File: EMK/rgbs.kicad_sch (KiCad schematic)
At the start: 0 parts

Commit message: feat: conclui a revisão 1 do EMK.
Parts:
- added C22, C23, C24, C25, C26, C27, C28, C29, C30, C31, C32, C33, C34, C35, C36, C37: 100nF, symbol Device:C
- added D20, D21, D22, D23, D24, D25, D26, D27, D28, D29, D30, D31, D32, D33, D34, D35: WS2812B, LED_SMD:LED_WS2812B_PLCC4_5.0x5.0mm_P3.2mm, symbol LED:WS2812B
- added D36: LED, symbol Device:LED
- added R12: 1K, symbol Device:R
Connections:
- new net: D33.2 (DOUT), D34.4 (DIN)
- new net: D32.2 (DOUT), D33.4 (DIN)
- new net: D20.2 (DOUT), D21.4 (DIN)
- new net: D27.2 (DOUT), D28.4 (DIN)
- new net: D26.2 (DOUT), D27.4 (DIN)
- new net: D36.2 (A), R12.1
- new net: D25.2 (DOUT), D26.4 (DIN)
- new net: D29.2 (DOUT), D30.4 (DIN)
- new net: D28.2 (DOUT), D29.4 (DIN)
- new net: D34.2 (DOUT), D35.4 (DIN)
- new net: D23.2 (DOUT), D24.4 (DIN)
- new net: D22.2 (DOUT), D23.4 (DIN)
- new net: D31.2 (DOUT), D32.4 (DIN)
- new net: D30.2 (DOUT), D31.4 (DIN)
- new net: D21.2 (DOUT), D22.4 (DIN)
- new net: D24.2 (DOUT), D25.4 (DIN)
- new net GND: C22.1, C23.1, C24.1, C25.1, C26.1, C27.1, C28.1, C29.1, C30.1, C31.1, C32.1, C33.1, C34.1, C35.1, C36.1, C37.1, D20.3 (VSS), D21.3 (VSS), D22.3 (VSS), D23.3 (VSS), D24.3 (VSS), D25.3 (VSS), D26.3 (VSS), D27.3 (VSS), D28.3 (VSS), D29.3 (VSS), D30.3 (VSS), D31.3 (VSS), D32.3 (VSS), D33.3 (VSS), D34.3 (VSS), D35.3 (VSS), D36.1 (K)
- new net ON_LED: R12.2
- new net RGB_SIG: D20.4 (DIN)
- new net RGB_VDD: C22.2, C23.2, C24.2, C25.2, C26.2, C27.2, C28.2, C29.2, C30.2, C31.2, C32.2, C33.2, C34.2, C35.2, C36.2, C37.2, D20.1 (VDD), D21.1 (VDD), D22.1 (VDD), D23.1 (VDD), D24.1 (VDD), D25.1 (VDD), D26.1 (VDD), D27.1 (VDD), D28.1 (VDD), D29.1 (VDD), D30.1 (VDD), D31.1 (VDD), D32.1 (VDD), D33.1 (VDD), D34.1 (VDD), D35.1 (VDD)

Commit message: Adiciona parte dos Footprints
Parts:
- C22, C23, C24, C25, C26, C27, C28, C29, C30, C31, C32, C33, C34, C35, C36, C37: footprint (none) -> Capacitor_SMD:C_0603_1608Metric
- D36: footprint (none) -> LED_SMD:LED_0603_1608Metric
- R12: footprint (none) -> Resistor_SMD:R_0603_1608Metric
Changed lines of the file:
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@@
 			)
 		)
-		(property "Footprint" ""
+		(property "Footprint" "Capacitor_SMD:C_0603_1608Metric"
 			(at 88.5952 64.77 0)
 			(effects
@@
 			)
 		)
-		(property "Footprint" ""
+		(property "Footprint" "Capacitor_SMD:C_0603_1608Metric"
 			(at 88.5952 101.6 0)
 			(effects
@@
 			)
 		)
-		(property "Footprint" ""
+		(property "Footprint" "Capacitor_SMD:C_0603_1608Metric"
 			(at 32.7152 138.43 0)
 			(effects
@@
 			)
 		)
-		(property "Footprint" ""
+		(property "Footprint" "Capacitor_SMD:C_0603_1608Metric"
 			(at 32.7152 64.77 0)
 			(effects
@@
 			)
 		)
-		(property "Footprint" ""
+		(property "Footprint" "Capacitor_SMD:C_0603_1608Metric"
 			(at 88.5952 27.94 0)
 			(effects
@@
 			)
 		)
-		(property "Footprint" ""
+		(property "Footprint" "Capacitor_SMD:C_0603_1608Metric"
 			(at 116.5352 27.94 0)
 			(effects
@@
 			)
 		)
-		(property "Footprint" ""
+		(property "Footprint" "LED_SMD:LED_0603_1608Metric"
 			(at 20.32 179.07 0)
 			(effects
@@
 			)
 		)
-		(property "Footprint" ""
+		(property "Footprint" "Capacitor_SMD:C_0603_1608Metric"
 			(at 60.6552 27.94 0)
 			(effects
@@
 			)
 		)
-		(property "Footprint" ""
+		(property "Footprint" "Capacitor_SMD:C_0603_1608Metric"
 			(at 60.6552 138.43 0)
 			(effects
@@
 			)
 		)
-		(property "Footprint" ""
+		(property "Footprint" "Capacitor_SMD:C_0603_1608Metric"
 			(at 60.6552 101.6 0)
 			(effects
@@
 			)
 		)
-		(property "Footprint" ""
+		(property "Footprint" "Capacitor_SMD:C_0603_1608Metric"
 			(at 116.5352 101.6 0)
 			(effects
@@
 			)
 		)
-		(property "Footprint" ""
+		(property "Footprint" "Capacitor_SMD:C_0603_1608Metric"
 			(at 32.7152 101.6 0)
 			(effects
@@
 			)
 		)
-		(property "Footprint" ""
+		(property "Footprint" "Resistor_SMD:R_0603_1608Metric"
 			(at 22.098 171.45 90)
 			(effects
@@
 			)
 		)
-		(property "Footprint" ""
+		(property "Footprint" "Capacitor_SMD:C_0603_1608Metric"
 			(at 88.5952 138.43 0)
 			(effects
@@
 			)
 		)
-		(property "Footprint" ""
+		(property "Footprint" "Capacitor_SMD:C_0603_1608Metric"
 			(at 60.6552 64.77 0)
 			(effects
@@
 			)
 		)
-		(property "Footprint" ""
+		(property "Footprint" "Capacitor_SMD:C_0603_1608Metric"
 			(at 32.7152 27.94 0)
 			(effects
@@
 			)
 		)
-		(property "Footprint" ""
+		(property "Footprint" "Capacitor_SMD:C_0603_1608Metric"
 			(at 116.5352 138.43 0)
 			(effects
@@
 			)
 		)
-		(property "Footprint" ""
+		(property "Footprint" "Capacitor_SMD:C_0603_1608Metric"
 			(at 116.5352 64.77 0)
 			(effects

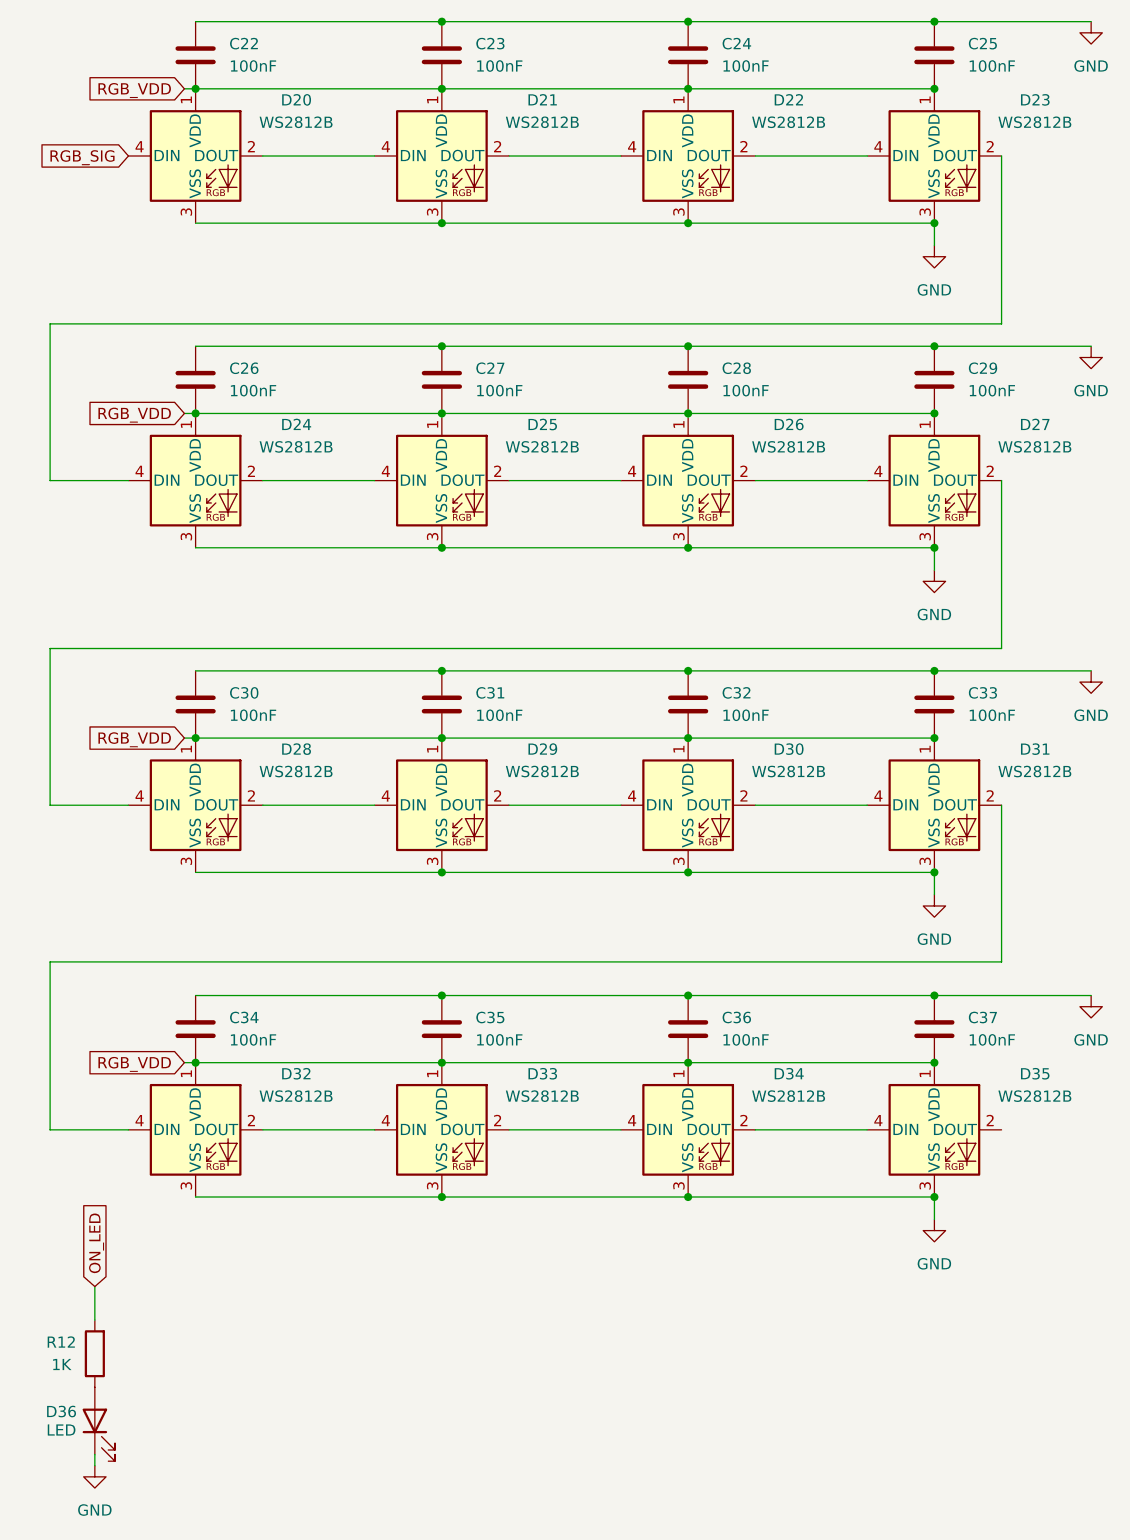
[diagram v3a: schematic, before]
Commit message: feat: realiza o roteamento das trilhas da matriz e dos leds.
Signed-off-by: Paulo Santos <prms@ic.ufal.br>
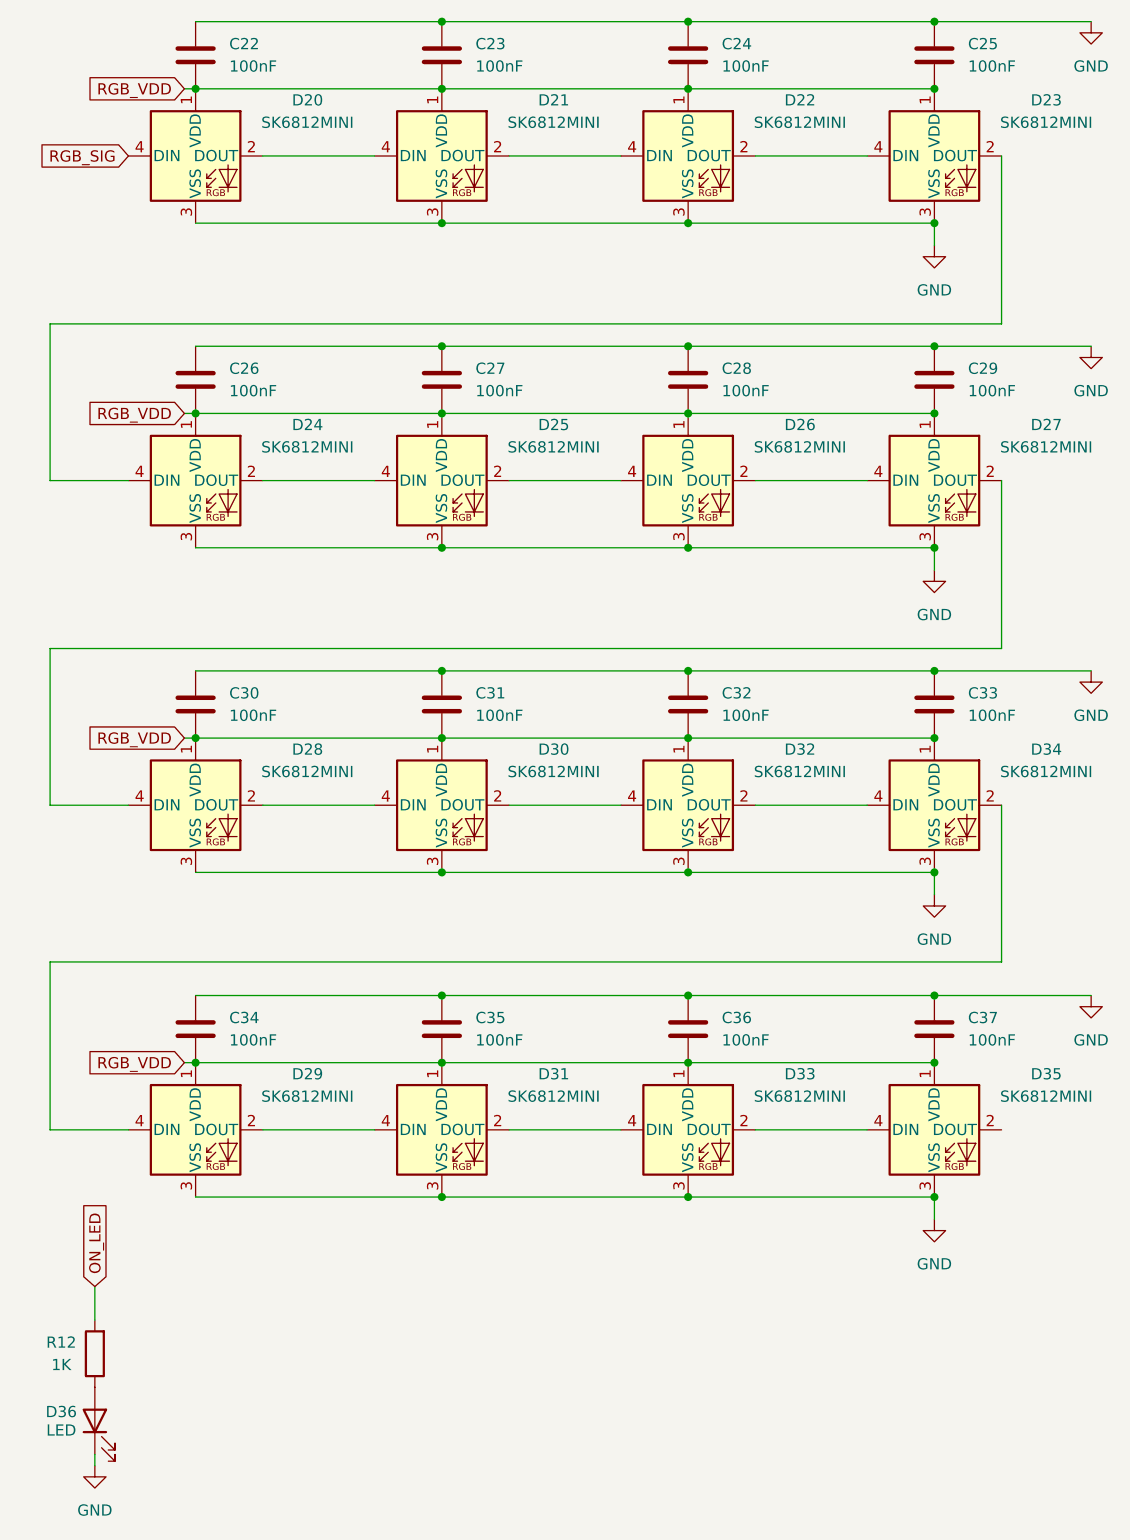
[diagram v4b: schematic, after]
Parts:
- removed D20, D21, D22, D23, D24, D25, D26, D27, D28, D29, D30, D31, D32, D33, D34, D35: WS2812B, LED_SMD:LED_WS2812B_PLCC4_5.0x5.0mm_P3.2mm, symbol LED:WS2812B
- added D20, D21, D22, D23, D24, D25, D26, D27, D28, D29, D30, D31, D32, D33, D34, D35: SK6812MINI, LED:SK6812MINI-E-PLCC4_3.2x2.8mm, symbol LED:SK6812MINI
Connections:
- net GND: now also D20.3 (VSS), D21.3 (VSS), D22.3 (VSS), D23.3 (VSS), D24.3 (VSS), D25.3 (VSS), D26.3 (VSS), D27.3 (VSS), D28.3 (VSS), D29.3 (VSS), D30.3 (VSS), D31.3 (VSS), D32.3 (VSS), D33.3 (VSS), D34.3 (VSS), D35.3 (VSS)
- net RGB_SIG: now also D20.4 (DIN)
- net RGB_VDD: now also D20.1 (VDD), D21.1 (VDD), D22.1 (VDD), D23.1 (VDD), D24.1 (VDD), D25.1 (VDD), D26.1 (VDD), D27.1 (VDD), D28.1 (VDD), D29.1 (VDD), D30.1 (VDD), D31.1 (VDD), D32.1 (VDD), D33.1 (VDD), D34.1 (VDD), D35.1 (VDD)
- new net: D25.2 (DOUT), D26.4 (DIN)
- new net: D24.2 (DOUT), D25.4 (DIN)
- new net: D32.2 (DOUT), D34.4 (DIN)
- new net: D30.2 (DOUT), D32.4 (DIN)
- new net: D23.2 (DOUT), D24.4 (DIN)
- new net: D22.2 (DOUT), D23.4 (DIN)
- new net: D21.2 (DOUT), D22.4 (DIN)
- new net: D20.2 (DOUT), D21.4 (DIN)
- new net: D26.2 (DOUT), D27.4 (DIN)
- new net: D28.2 (DOUT), D30.4 (DIN)
- new net: D27.2 (DOUT), D28.4 (DIN)
- new net: D33.2 (DOUT), D35.4 (DIN)
- new net: D29.4 (DIN), D34.2 (DOUT)
- new net: D29.2 (DOUT), D31.4 (DIN)
- new net: D31.2 (DOUT), D33.4 (DIN)
